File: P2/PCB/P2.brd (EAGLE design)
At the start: 98.7 x 30.5 mm, 28 parts, among them CON1 Volume, CON2 Noritake, IC1 ATMEGA48/88/168-AU, IC2 TPIC6B595DW, IC3 TPIC6B595DW, K1 G6H2-100, Q1 16MHz

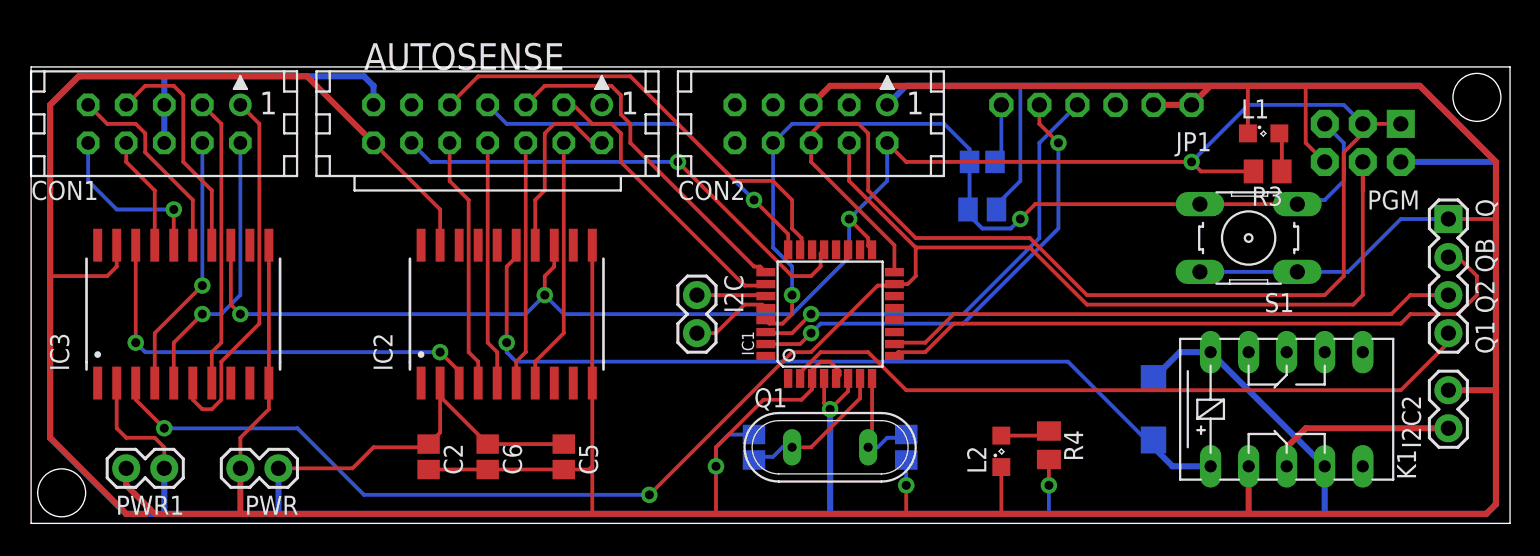
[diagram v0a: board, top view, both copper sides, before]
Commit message: Added AutoSense, missing connections on P2
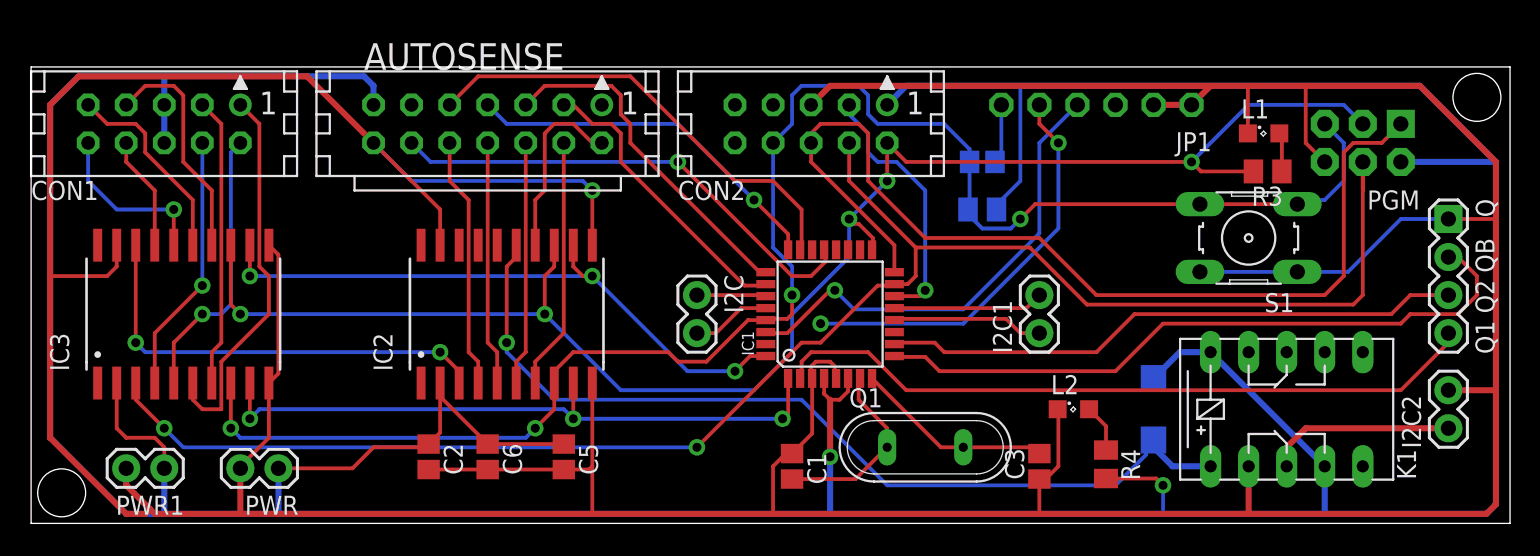
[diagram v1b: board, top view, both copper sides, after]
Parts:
- added I2C1: pb0 pb1, SparkFun:1X02
- moved C3 8.98 mm to (67.3, 3.81), flipped to the top
- moved Q1 6.35 mm to (59.7, 5.08)
- moved L2 5.57 mm to (69.6, 7.62), turned to 0 degrees
- moved R4 4.02 mm to (71.8, 3.94)
- moved C1 2.84 mm to (50.8, 3.81), flipped to the top
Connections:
- removed net D8: CON2.3
- removed net N$14: AUTOSENSE.11
- new net G: IC1.1, IC2.9, IC3.9
- new net RCK: IC1.32, IC2.12, IC3.12
- new net SS: CON2.3, IC1.14
- net PB0: now also I2C1.1
- net PB1: now also I2C1.2
- net RESET: now also IC2.8, IC3.8
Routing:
- net RESET: track 64.2 -> 112.3 mm, vias 2 -> 4
- net G: track 0.00 -> 43.7 mm, vias 0 -> 3
- net RCK: track 0.00 -> 42.5 mm, vias 0 -> 3
- net SS: track 0.00 -> 17.4 mm, vias 0 -> 1
- net PB0: track 0.00 -> 10.1 mm
- net PB1: track 0.00 -> 10.0 mm
- net SCK: track 101.9 -> 108.0 mm, vias 4 -> 5
- net N$2: track 7.60 -> 13.2 mm
- net GND: track 350.9 -> 356.5 mm, vias 2 -> 1
- net N$4: track 31.5 -> 27.3 mm
- net OUT13: track 57.8 -> 60.9 mm
- net MOSI: track 115.2 -> 112.6 mm
- net N$1: track 10.1 -> 12.7 mm
- net +5V: track 303.6 -> 305.6 mm
- net OUT2: track 24.8 -> 25.7 mm
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
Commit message: Jumper for IR and SS, silkscreen cleanups.
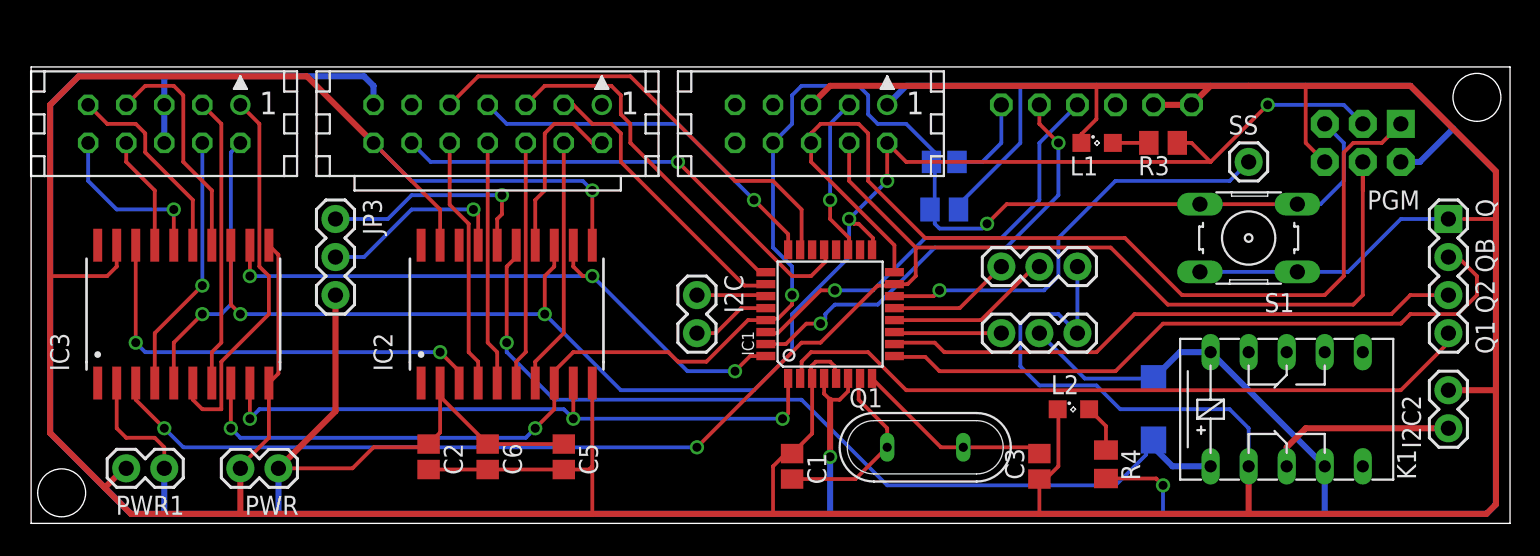
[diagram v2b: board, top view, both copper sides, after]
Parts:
- removed AUTOSENSE: (no value), con-harting-lars:CON14L
- removed I2C1: pb0 pb1, SparkFun:1X02
- added CON3: Noritake, con-harting-lars:CON10L
- added JP2: pb1 pb0 gnd, SparkFun-Connectors:1X03
- added JP3: (no value), SparkFun-Connectors:1X03
- added JP4: ir, SparkFun-Connectors:1X03
- added SS: M01PTH, SparkFun-Connectors:1X01
- CON2: value Noritake -> Autosense; device con-harting-lars:CON10L -> con-harting-lars:CON14L
- I2C2: value power -> pwsw
- moved CON2 21.6 mm to (30.5, 26.7)
- moved L1 11.1 mm to (71.2, 25.4)
- moved R3 7.24 mm to (75.6, 25.4), turned to 0 degrees
- moved C4 2.54 mm to (61.0, 24.1)
- moved R1 2.54 mm to (61.0, 21.0)
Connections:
- removed net PB0: I2C1.1, IC1.12
- removed net PB1: I2C1.2, IC1.13
- new net N$10: IC1.12, JP2.2
- new net N$11: IC2.16, JP3.1
- new net N$12: IC2.17, JP3.2
- new net N$14: IC1.11, JP4.1
- new net N$9: IC1.13, JP2.1
- new net PC6: CON3.3, IC1.19
- net +5V: now also CON2.13, CON3.1, JP3.3, JP4.2; no longer AUTOSENSE.13, CON2.1
- net ADC0: now also CON2.9; no longer AUTOSENSE.9
- net ADC1: now also CON2.7; no longer AUTOSENSE.7
- net ADC2: now also CON2.5; no longer AUTOSENSE.5
- net ADC3: now also CON2.3; no longer AUTOSENSE.3
- net AGND: now also CON2.12; no longer AUTOSENSE.12
- net GND: now also CON2.14, CON3.5, JP2.3, JP4.3; no longer AUTOSENSE.14, CON2.5
- net MISO: now also CON3.6; no longer CON2.6
- net MOSI: now also CON3.4; no longer CON2.4
- net OUT10: now also CON2.6; no longer AUTOSENSE.6
- net OUT11: now also CON2.4; no longer AUTOSENSE.4
- net OUT12: now also CON2.2; no longer AUTOSENSE.2
- net OUT8: now also CON2.10; no longer AUTOSENSE.10
- net OUT9: now also CON2.8; no longer AUTOSENSE.8
- net RESET: now also CON3.8; no longer CON2.8
- net SCK: now also CON3.2; no longer CON2.2
- net SS: now also SS.1; no longer CON2.3
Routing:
- net GND: track 356.5 -> 386.8 mm
- net +5V: track 305.6 -> 326.2 mm
- net N$11: track 0.00 -> 15.2 mm, vias 0 -> 1
- net N$12: track 0.00 -> 13.0 mm, vias 0 -> 1
- net SS: track 17.4 -> 28.8 mm
- net PC6: track 0.00 -> 11.3 mm, vias 0 -> 1
- net N$10: track 0.00 -> 11.2 mm
- net PB0: track 10.1 -> 0.00 mm
- net PB1: track 10.0 -> 0.00 mm
- net N$9: track 0.00 -> 8.29 mm
- net N$14: track 0.00 -> 7.17 mm
- net N$4: track 27.3 -> 30.4 mm
- net RTS#: track 3.98 -> 6.03 mm
- net N$3: track 31.7 -> 29.7 mm
- net SCK: track 108.0 -> 106.4 mm

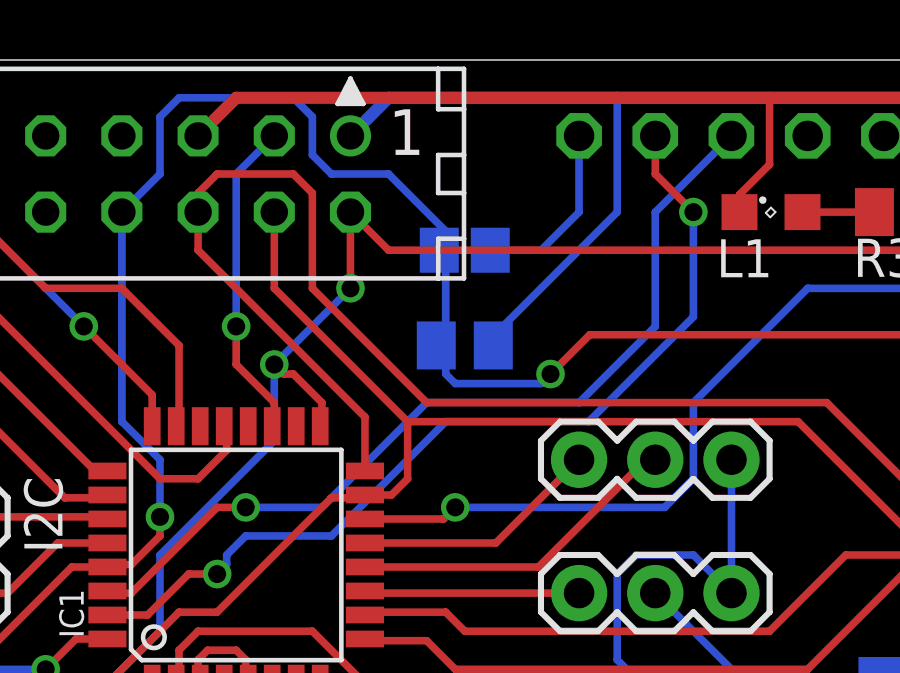
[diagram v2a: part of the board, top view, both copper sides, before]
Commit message: Connect AVCC
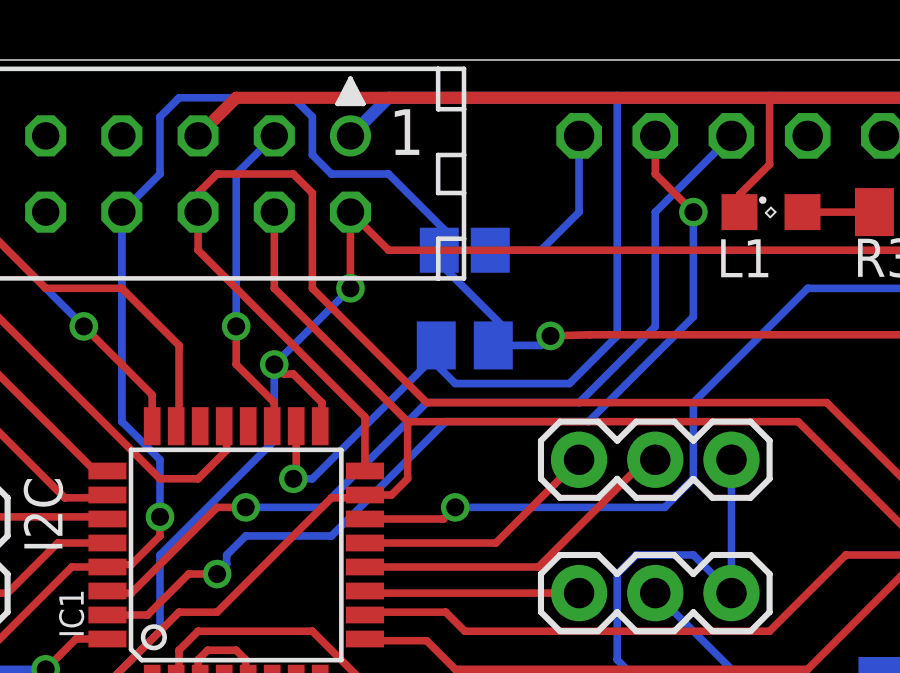
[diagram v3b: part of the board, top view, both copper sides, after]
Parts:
- turned R1 to 180 degrees
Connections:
- net +5V: now also IC1.18
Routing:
- net +5V: track 326.2 -> 340.5 mm, vias 2 -> 3
- net RESET: track 112.3 -> 109.6 mm
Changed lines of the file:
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@@
 </autorouter>
 <elements>
-<element name="R1" library="resistor" package="M0805" value="10K" x="60.96" y="20.955" smashed="yes" rot="MR0">
-<attribute name="NAME" x="65.786" y="20.701" size="1.27" layer="26" rot="MR0"/>
-<attribute name="VALUE" x="58.801" y="20.2565" size="1.27" layer="28" rot="MR0"/>
+<element name="R1" library="resistor" package="M0805" value="10K" x="60.96" y="20.955" smashed="yes" rot="MR180">
+<attribute name="NAME" x="56.134" y="21.209" size="1.27" layer="26" rot="MR180"/>
+<attribute name="VALUE" x="63.119" y="21.6535" size="1.27" layer="28" rot="MR180"/>
 </element>
 <element name="C2" library="resistor" package="C0805" value="0.1uF" x="26.535" y="4.445" rot="R270"/>
@@
 <wire x1="66.04" y1="29.21" x2="58.42" y2="29.21" width="0.4064" layer="16"/>
 <wire x1="58.42" y1="29.21" x2="57.15" y2="27.94" width="0.4064" layer="16"/>
-<wire x1="66.04" y1="25.4" x2="66.04" y2="29.21" width="0.254" layer="16"/>
 <wire x1="16.51" y1="3.675" x2="21.455" y2="3.675" width="0.254" layer="1"/>
 <wire x1="21.455" y1="3.675" x2="22.86" y2="5.08" width="0.254" layer="1"/>
@@
 <wire x1="20.32" y1="7.485" x2="16.51" y2="3.675" width="0.4064" layer="1"/>
 <contactref element="JP4" pad="2"/>
-<wire x1="61.91" y1="20.955" x2="61.91" y2="21.27" width="0.254" layer="16"/>
-<wire x1="61.91" y1="21.27" x2="66.04" y2="25.4" width="0.254" layer="16"/>
 <wire x1="74.93" y1="9.67" x2="70.34" y2="9.67" width="0.254" layer="16"/>
 <wire x1="70.34" y1="9.67" x2="67.31" y2="12.7" width="0.254" layer="16"/>
+<contactref element="IC1" pad="18"/>
+<wire x1="66.04" y1="29.21" x2="66.04" y2="21.2725" width="0.254" layer="16"/>
+<wire x1="66.04" y1="21.2725" x2="64.4525" y2="19.685" width="0.254" layer="16"/>
+<wire x1="64.4525" y1="19.685" x2="60.6425" y2="19.685" width="0.254" layer="16"/>
+<wire x1="60.6425" y1="19.685" x2="60.0075" y2="20.32" width="0.254" layer="16"/>
+<wire x1="60.0075" y1="20.32" x2="60.0075" y2="20.9525" width="0.254" layer="16"/>
+<wire x1="60.0075" y1="20.9525" x2="60.01" y2="20.955" width="0.254" layer="16"/>
+<wire x1="60.01" y1="20.955" x2="59.69" y2="20.955" width="0.254" layer="16"/>
+<via x="55.245" y="16.51" extent="1-16" drill="0.6"/>
+<wire x1="55.34" y1="18.2626" x2="55.34" y2="16.605" width="0.254" layer="1"/>
+<wire x1="55.34" y1="16.605" x2="55.245" y2="16.51" width="0.254" layer="1"/>
+<wire x1="59.69" y1="20.955" x2="59.69" y2="20.32" width="0.254" layer="16"/>
+<wire x1="59.69" y1="20.32" x2="55.88" y2="16.51" width="0.254" layer="16"/>
+<wire x1="55.88" y1="16.51" x2="55.245" y2="16.51" width="0.254" layer="16"/>
 </signal>
 <signal name="MOSI">
@@
 <wire x1="87.63" y1="22.86" x2="86.0806" y2="21.3106" width="0.254" layer="16"/>
 <wire x1="78.0288" y1="21.3106" x2="84.5312" y2="21.3106" width="0.254" layer="1"/>
-<wire x1="63.8175" y1="20.0025" x2="63.5" y2="19.685" width="0.254" layer="16"/>
-<via x="63.8175" y="20.0025" extent="1-16" drill="0.6"/>
+<via x="63.8175" y="21.2725" extent="1-16" drill="0.6"/>
 <wire x1="78.0288" y1="21.3106" x2="65.1256" y2="21.3106" width="0.254" layer="1"/>
 <wire x1="50.8" y1="17.145" x2="50.8" y2="15.24" width="0.254" layer="16"/>
@@
 <wire x1="56.515" y1="26.67" x2="58.42" y2="26.67" width="0.254" layer="16"/>
 <wire x1="58.42" y1="26.67" x2="60.325" y2="24.765" width="0.254" layer="16"/>
-<wire x1="60.325" y1="24.345" x2="60.325" y2="21.27" width="0.254" layer="16"/>
-<wire x1="60.325" y1="21.27" x2="60.01" y2="20.955" width="0.254" layer="16"/>
 <wire x1="60.325" y1="24.765" x2="60.325" y2="24.345" width="0.254" layer="16"/>
 <wire x1="60.325" y1="24.345" x2="60.11" y2="24.13" width="0.254" layer="16"/>
-<wire x1="63.5" y1="19.685" x2="60.6425" y2="19.685" width="0.254" layer="16"/>
-<wire x1="60.6425" y1="19.685" x2="60.325" y2="20.0025" width="0.254" layer="16"/>
-<wire x1="60.325" y1="20.0025" x2="60.325" y2="20.64" width="0.254" layer="16"/>
-<wire x1="60.325" y1="20.64" x2="60.01" y2="20.955" width="0.254" layer="16"/>
-<wire x1="65.1256" y1="21.3106" x2="63.8175" y2="20.0025" width="0.254" layer="1"/>
+<wire x1="65.1256" y1="21.3106" x2="63.8175" y2="21.2725" width="0.254" layer="1"/>
+<wire x1="60.11" y1="24.13" x2="60.11" y2="23.71" width="0.254" layer="16"/>
+<wire x1="60.11" y1="23.71" x2="62.23" y2="21.59" width="0.254" layer="16"/>
+<wire x1="62.23" y1="21.59" x2="62.23" y2="21.275" width="0.254" layer="16"/>
+<wire x1="62.23" y1="21.275" x2="61.91" y2="20.955" width="0.254" layer="16"/>
+<wire x1="61.91" y1="20.955" x2="63.5" y2="20.955" width="0.254" layer="16"/>
+<wire x1="63.5" y1="20.955" x2="63.8175" y2="21.2725" width="0.254" layer="16"/>
 </signal>
 <signal name="QE1">
@@
 </signal>
 </signals>
-<errors>
-</errors>
 </board>
 </drawing>
